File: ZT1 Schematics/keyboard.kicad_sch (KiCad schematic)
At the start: 25 parts, among them Q102 2N3904, U108 74LS00, U115 74LS32, U121 74156, U122 74LS368, U123 74LS368

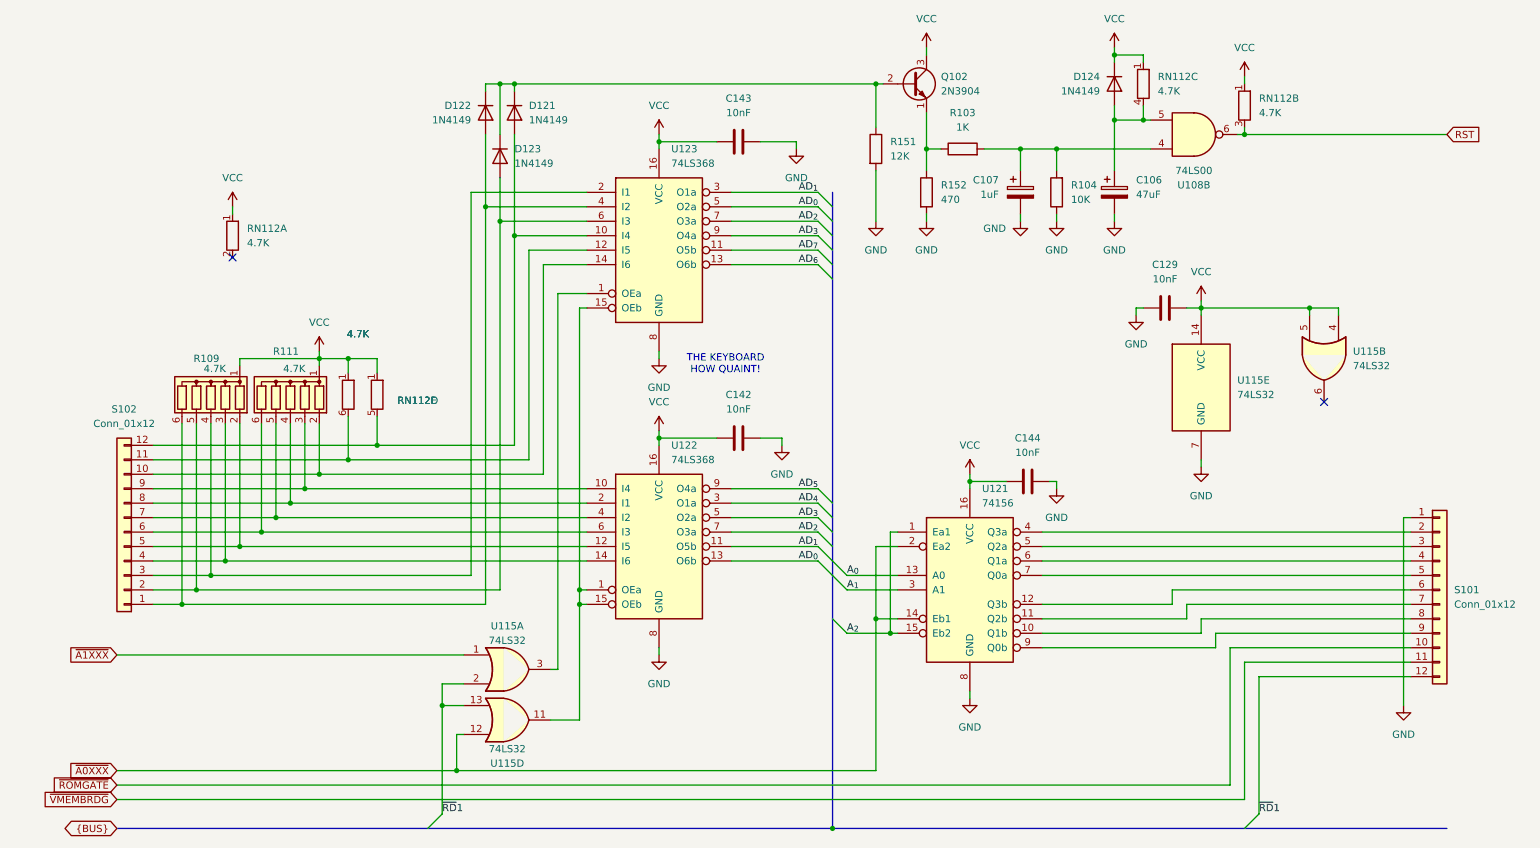
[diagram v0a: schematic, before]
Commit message: Minor touchups
Fixed some of the text
Added some explanations
Simplified the video circuit
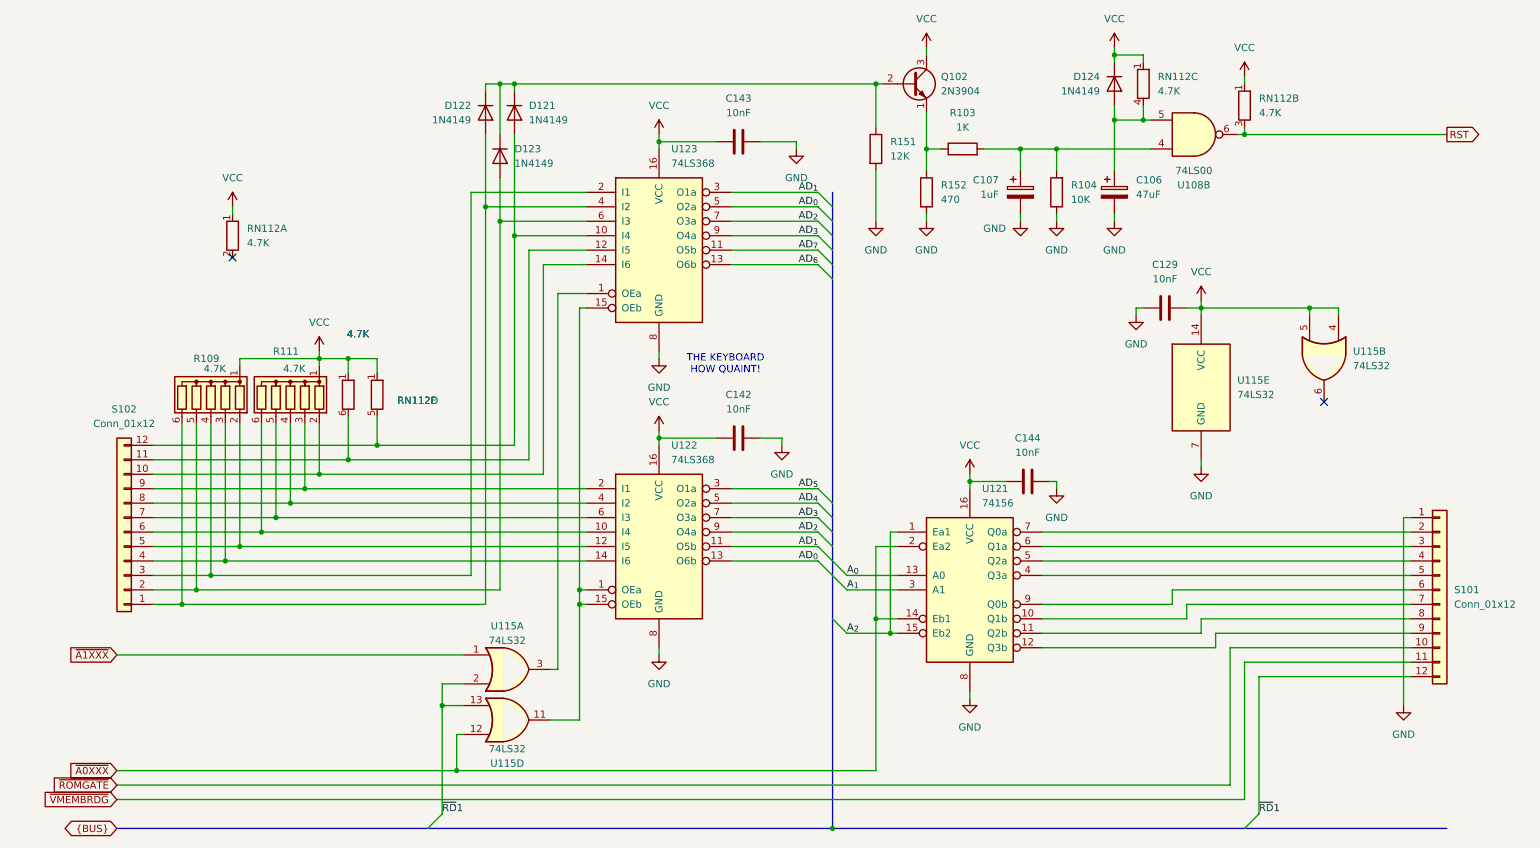
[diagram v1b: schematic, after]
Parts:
- C106, C107: footprint ZX1:CP_Radial_D5.0mm_P2.50mm -> ZT1:CP_Radial_D5.0mm_P2.50mm
- C129, C142, C143, C144: footprint ZX1:C_350mil -> ZT1:C_350mil
- D121, D122, D123, D124: footprint ZX1:D_350mil -> ZT1:D_350mil
- Q102: footprint Package_TO_SOT_THT:TO-92L_Inline_Wide -> Package_TO_SOT_THT:TO-92_Inline
- R103, R104, R151, R152: footprint ZX1:R_450mil -> ZT1:R_450mil
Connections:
- net AD_{2}: now also U122.9 (O4a); no longer U122.7 (O3a)
- net AD_{3}: now also U122.7 (O3a); no longer U122.5 (O2a)
- net AD_{4}: now also U122.5 (O2a); no longer U122.3 (O1a)
- net AD_{5}: now also U122.3 (O1a); no longer U122.9 (O4a)
- net at S101.2 (Pin_2): now also U121.7 (Q0a); no longer U121.4 (Q3a)
- net at S101.3 (Pin_3): now also U121.6 (Q1a); no longer U121.5 (Q2a)
- net at S101.4 (Pin_4): now also U121.5 (Q2a); no longer U121.6 (Q1a)
- net at S101.5 (Pin_5): now also U121.4 (Q3a); no longer U121.7 (Q0a)
- net at S101.6 (Pin_6): now also U121.9 (Q0b); no longer U121.12 (Q3b)
- net at S101.7 (Pin_7): now also U121.10 (Q1b); no longer U121.11 (Q2b)
- net at S101.8 (Pin_8): now also U121.11 (Q2b); no longer U121.10 (Q1b)
- net at S101.9 (Pin_9): now also U121.12 (Q3b); no longer U121.9 (Q0b)
- net at R111.3 (R2), S102.9 (Pin_9): now also U122.2 (I1); no longer U122.10 (I4)
- net at R111.4 (R3), S102.8 (Pin_8): now also U122.4 (I2); no longer U122.2 (I1)
- net at R111.5 (R4), S102.7 (Pin_7): now also U122.6 (I3); no longer U122.4 (I2)
- net at R111.6 (R5), S102.6 (Pin_6): now also U122.10 (I4); no longer U122.6 (I3)
